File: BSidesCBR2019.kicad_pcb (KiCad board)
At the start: 2 copper layers, 44.9 x 114.1 mm, 38 parts, among them IC1 Si4455-B1A-FM, J1 SAO, J2 LSAO, SW1 RESET, U1 ATMEGA328P-AU, U2 Nokia_5110_LCD, Y1 16Mhz, Y2 30Mhz

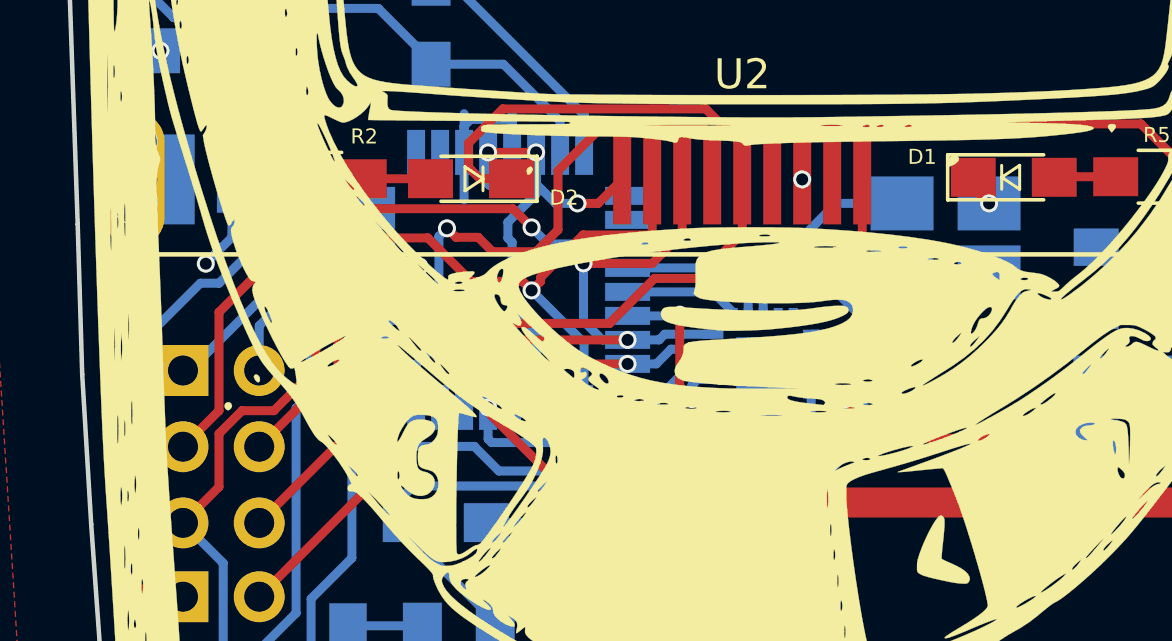
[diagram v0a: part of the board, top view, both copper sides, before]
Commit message: Regen gerbers and update footprint for si4455
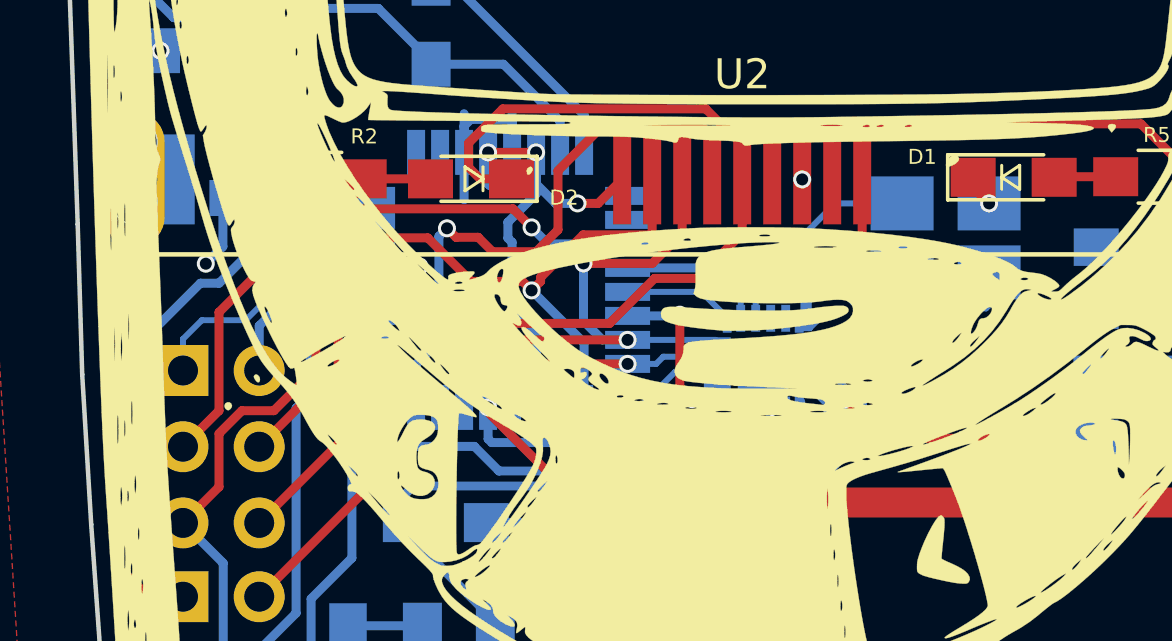
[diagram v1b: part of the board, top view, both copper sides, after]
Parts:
- BT1: value Battery_Cell -> CR2450
- D5: footprint Diodes_SMD:D_SOD-323_HandSoldering -> Diodes_SMD:D_SOD-123
- IC1: footprint Si4455-B1A-FM:QFN50P300X300X80-21N-D -> Silicon Labs - Si4455-B1A-FM:SILICON_LABS_SI4455-B1A-FM_0
- moved D5 0.10 mm to (43.4, 103.2)
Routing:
- net +3.3v: track 34.3 -> 27.0 mm, vias 13 -> 14
- net GND: track 36.5 -> 39.5 mm
- net /XIN: track 9.84 -> 11.1 mm
- net TXD: track 9.41 -> 10.2 mm
- net /TXA: track 31.7 -> 32.4 mm
- net RESET: track 80.3 -> 80.8 mm
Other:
- net class Thinz added: clearance 0.2, trace_width 0.2, via_dia 0.4, via_drill 0.3

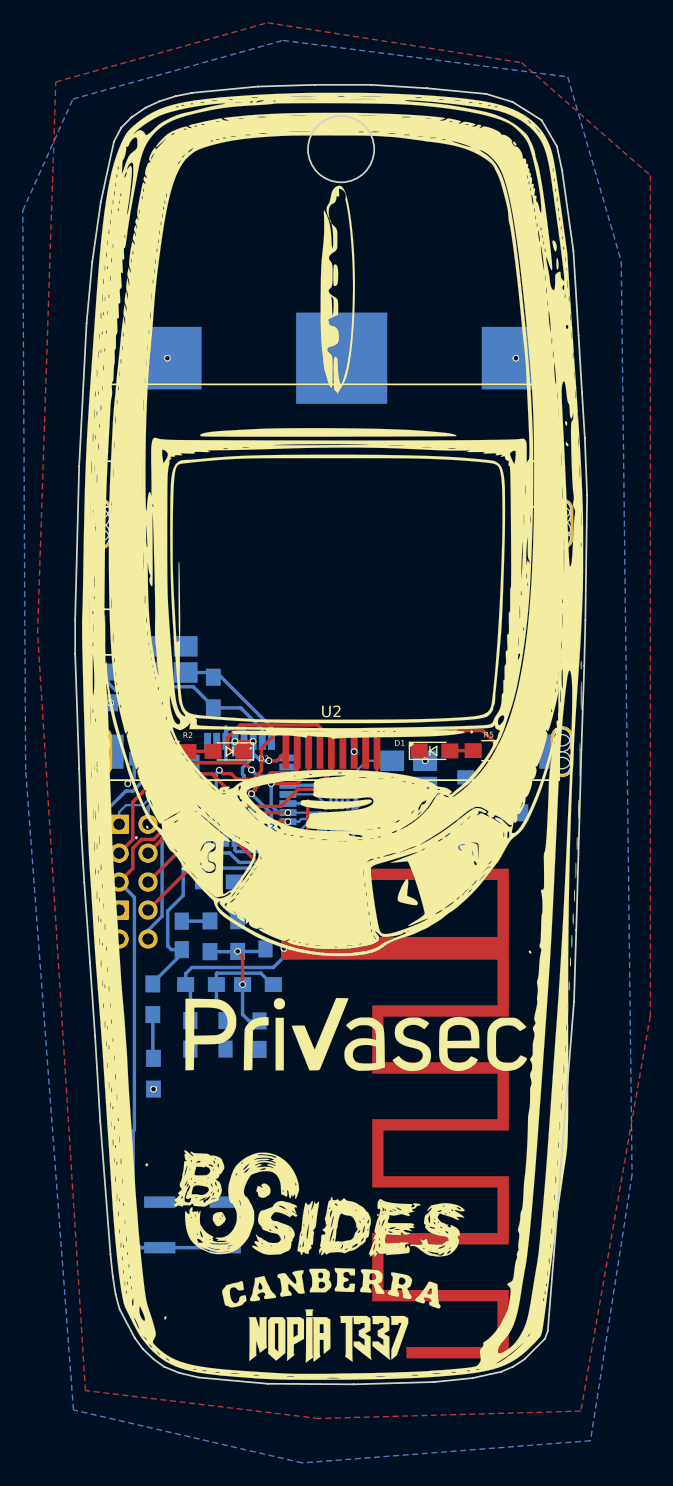
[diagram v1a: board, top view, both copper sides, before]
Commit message: Added each gerber revision, updated with latest version of board designs.
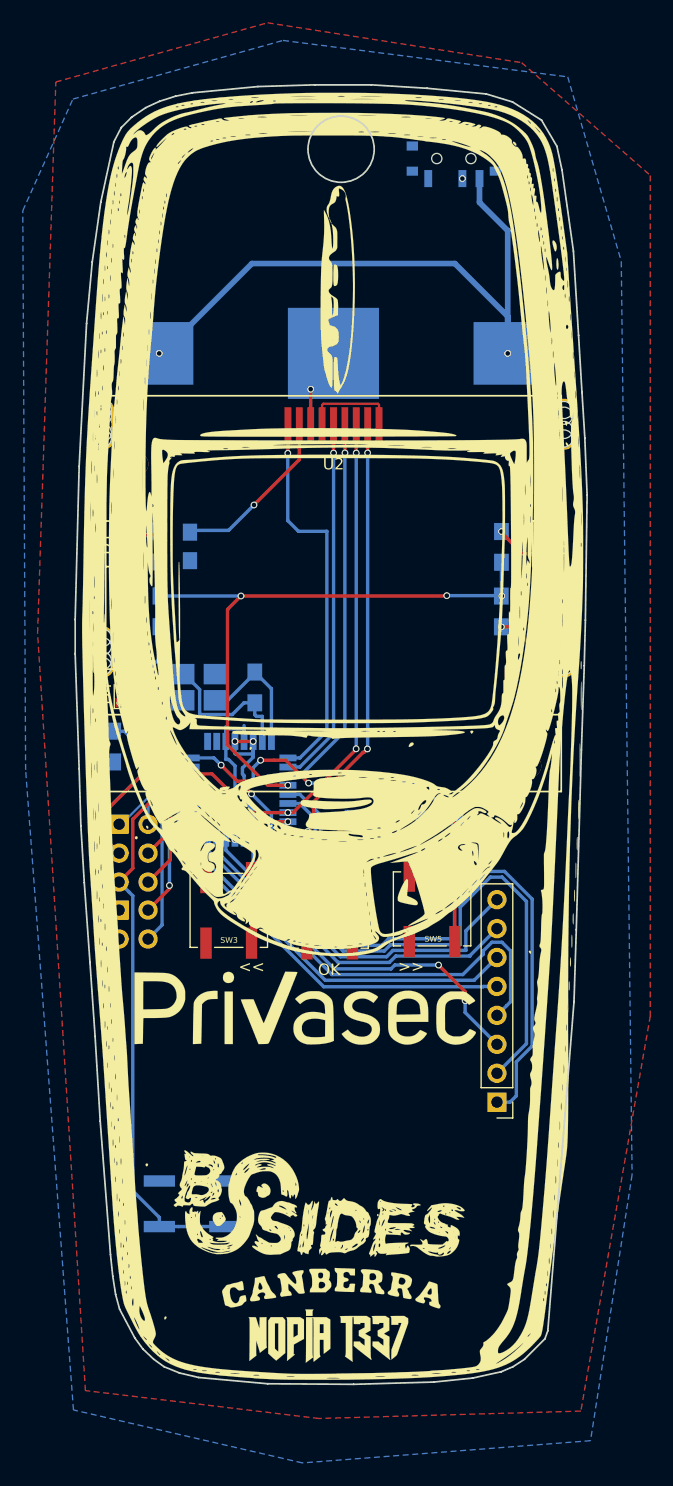
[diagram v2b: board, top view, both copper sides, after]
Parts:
- removed AE1: Antenna_Dipole, dipole:ti-dn023-antenna
- removed C0, C2, C3, C4, CM1, CM2, CM3, CR1, CR2: , Capacitors_SMD:C_0805_HandSoldering
- removed D5: 1N4148, Diodes_SMD:D_SOD-123
- removed the G*** at (41.9, 114.0)
- removed the G*** at (61.3, 127.4)
- removed IC1: Si4455-B1A-FM, Silicon Labs - Si4455-B1A-FM:SILICON_LABS_SI4455-B1A-FM_0
- removed L0, LM1, LM2, LR1, LR2, Lchoke1: , Inductors_SMD:L_0805_HandSoldering
- removed ROC1: , Resistors_SMD:R_0805_HandSoldering
- removed Y2: 30Mhz, Crystals:Crystal_SMD_TXC_7M-4pin_3.2x2.5mm_HandSoldering
- added D3: BL, LEDs:LED_0603, F.Cu at (78.0, 97.3)
- added D4: BL, LEDs:LED_0603, F.Cu at (40.5, 97.5)
- added G***: LOGO, LOGO, B.Cu at (42.1, 114.0)
- added G***: LOGO, LOGO, F.Cu at (56.8, 125.1)
- added J3: IO, Pin_Headers:Pin_Header_Straight_1x08_Pitch2.54mm, F.Cu at (73.6, 133.3)
- added POWER: SW_SPST, Buttons_Switches_SMD:SW_SPDT_PCM12, B.Cu at (69.8, 50.8)
- added R6: LR, Resistors_SMD:R_0805_HandSoldering, B.Cu at (44.0, 90.2)
- added R7: 1k, Resistors_SMD:R_0805_HandSoldering, B.Cu at (62.4, 108.3)
- added R8: 1k, Resistors_SMD:R_0805_HandSoldering, B.Cu at (68.6, 108.4)
- added R9: 1K, Resistors_SMD:R_0805_HandSoldering, B.Cu at (40.0, 102.1)
- added SW3: <<, Buttons_Switches_SMD:SW_SPST_B3SL-1002P, F.Cu at (50.1, 116.5)
- added SW4: OK, Buttons_Switches_SMD:SW_SPST_B3SL-1002P, F.Cu at (58.9, 116.6)
- added SW5: >>, Buttons_Switches_SMD:SW_SPST_B3SL-1002P, F.Cu at (67.9, 116.4)
- BT1: value CR2450 -> CR2032
- C1: value (none) -> 100n
- D1, D2: footprint LEDs:LED_0805_HandSoldering -> LEDs:LED_0603
- R2, R5: moved to B.Cu
- R3: value 1K -> LR
- R4: value 1M -> 10K
- moved C1 36.5 mm to (46.7, 84.5)
- moved U2 33.8 mm to (59.3, 71.3), turned to 0 degrees
- moved D2 33.3 mm to (78.0, 84.4), turned to 270 degrees
- moved D1 33.1 mm to (40.5, 84.3), turned to 90 degrees
- moved R3 32.0 mm to (74.0, 90.2), turned to 270 degrees
- moved R2 18.0 mm to (44.0, 84.5), turned to 90 degrees
- moved R5 17.9 mm to (74.0, 84.6), turned to 90 degrees
- moved R4 5.74 mm to (42.8, 101.8), turned to 90 degrees
- moved R1 3.67 mm to (52.4, 96.9)
- moved Y1 3.59 mm to (47.5, 96.9)
- moved SW1 1.85 mm to (46.9, 142.2)
- moved BT1 0.83 mm to (59.3, 67.6)
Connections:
- net Net-(U1-Pad1) renamed D3
- net Net-(U1-Pad2) renamed D4
- BT1 pad 1: +3.3v -> BAT+
- C1 pad 1: +3.3v -> /VOUT
- D2 pad 1: Net-(D2-Pad1) -> GND
- R2 pad 1: Net-(D2-Pad2) -> LCDBL+
- R2 pad 2: LCDBL+ -> Net-(D1-Pad2)
- R3 pad 1: RESET -> LCDBL+
- R3 pad 2: GND -> Net-(D3-Pad2)
- R5 pad 1: Net-(D2-Pad1) -> LCDBL+
- R5 pad 2: Net-(D1-Pad2) -> Net-(D2-Pad2)
- U1 pad 10: Net-(U1-Pad10) -> LCDCE
- U1 pad 11: LCDBL+ -> LCDDC
- U1 pad 12: LCDRST -> LCDBL+
- U1 pad 13: RFNSEL -> D9
- U1 pad 14: RFNIRQ -> D10
- U1 pad 19: Net-(U1-Pad19) -> A6
- U1 pad 22: Net-(U1-Pad22) -> A7
- U1 pad 23: Net-(U1-Pad23) -> AD0
- U1 pad 24: LCDCE -> AD1
- U1 pad 25: Net-(U1-Pad25) -> AD2
- U1 pad 26: LCDDC -> AD3
- U1 pad 32: Net-(U1-Pad32) -> BUTTONS
- U1 pad 9: Net-(U1-Pad9) -> LCDRST
- U2 pad 2: Net-(U2-Pad2) -> /VOUT
- U2 pad 4: Net-(U2-Pad4) -> +3.3v
- Y1 pad 4: (no net) -> GND
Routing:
- net D9: track 0.00 -> 60.1 mm
- net D10: track 0.00 -> 55.9 mm
- net BAT+: track 0.00 -> 55.4 mm, vias 0 -> 2
- net BUTTONS: track 0.00 -> 46.2 mm, vias 0 -> 5
- net LCDBL+: track 12.4 -> 56.4 mm, vias 1 -> 4
- net AD1: track 0.00 -> 40.0 mm
- net AD3: track 0.00 -> 36.9 mm
- net AD2: track 0.00 -> 35.0 mm
- net AD0: track 0.00 -> 34.1 mm, vias 0 -> 2
- net /TXA: track 32.4 -> 0.00 mm
- net SCK: track 33.4 -> 65.1 mm, vias 2 -> 5
- net /RXN: track 30.5 -> 0.00 mm, vias 2 -> 0
- net A6: track 0.00 -> 30.4 mm
- net A7: track 0.00 -> 30.2 mm
- net Net-(D2-Pad1): track 28.1 -> 0.00 mm
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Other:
- net class SupaThicc added: clearance 0.5, trace_width 1, via_dia 0.6, via_drill 0.4
- board text added: "A6"
- board text added: "A7"
- board text added: "AD0"
- board text added: "AD1"
- board text added: "AD2"
- board text added: "AD3"
- board text added: "D10"
- board text added: "D9"
- board text added: "ec0 (ĕ'kō) csirac2 Peter"
- board text removed: "ĕ'kō (ec0) csirac2 Peter"
